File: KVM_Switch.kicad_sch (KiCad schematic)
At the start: 4 parts, among them J1 HDMI_A, J2 HDMI_A, U1 USB2514B_Bi, U2 STM32C011F4Px

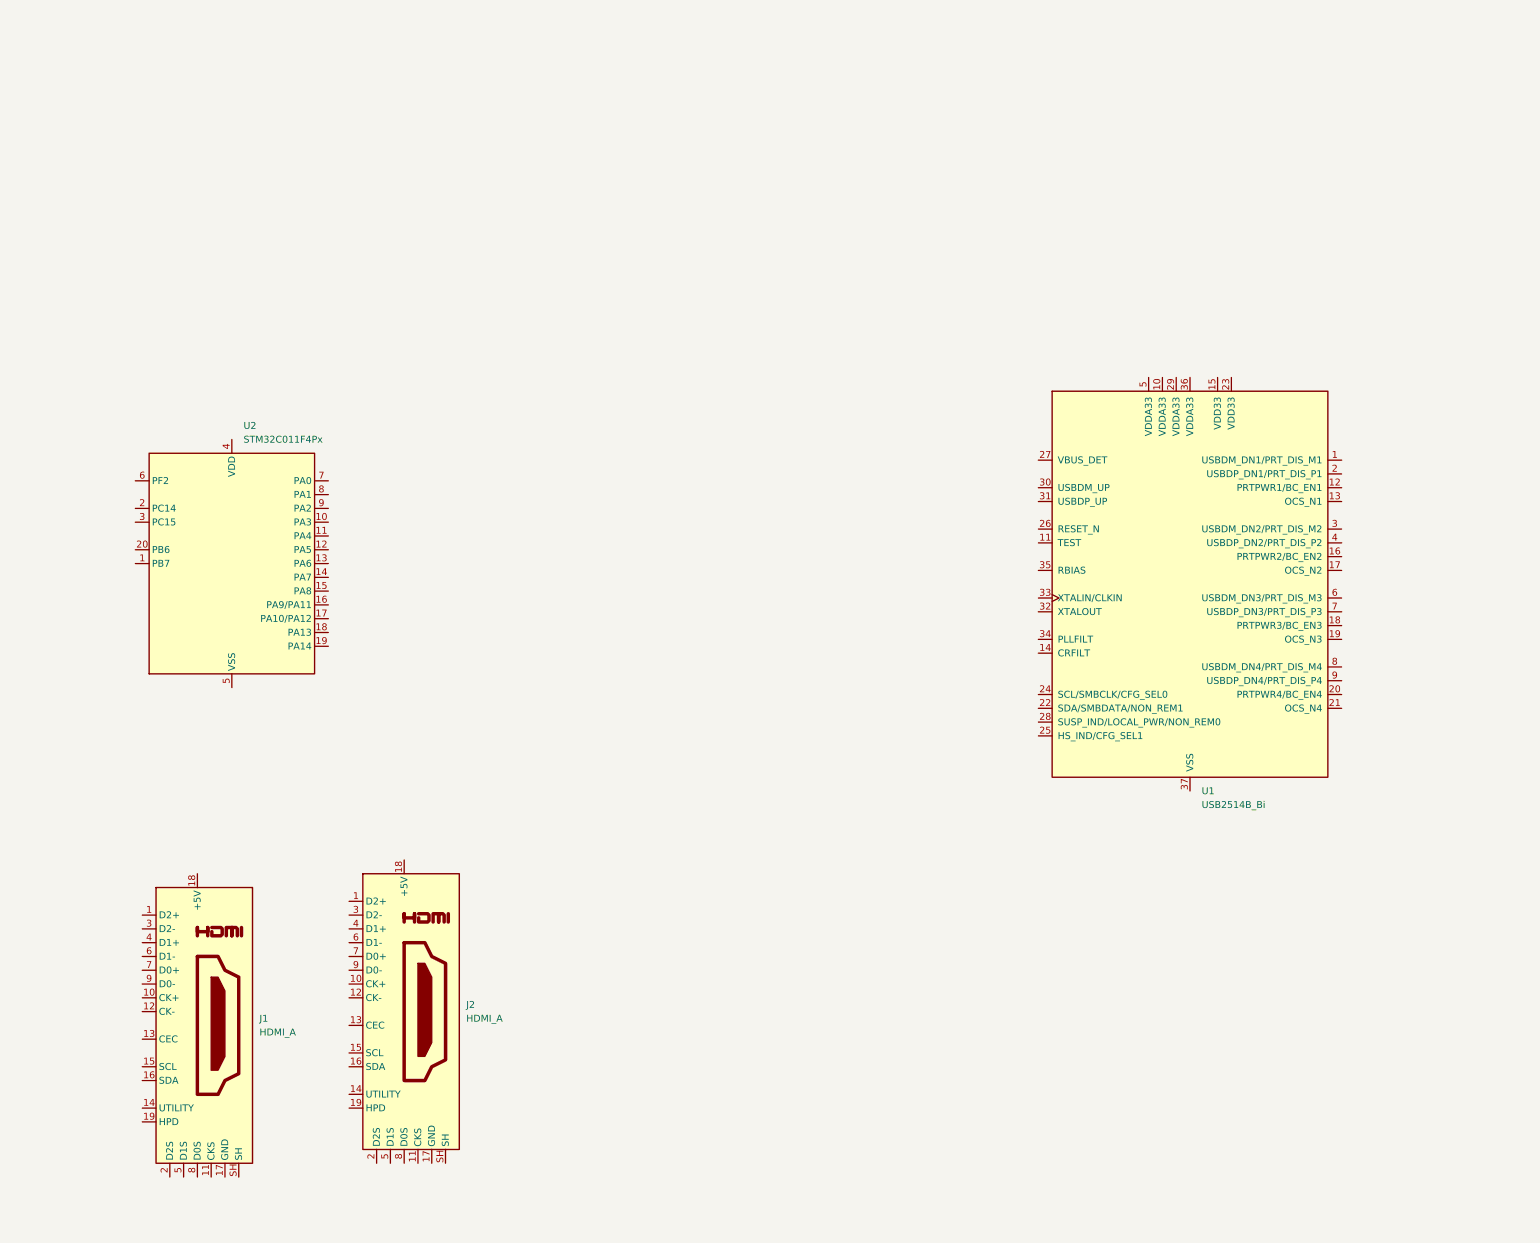
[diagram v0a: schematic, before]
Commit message: Added switching ICs and MCU
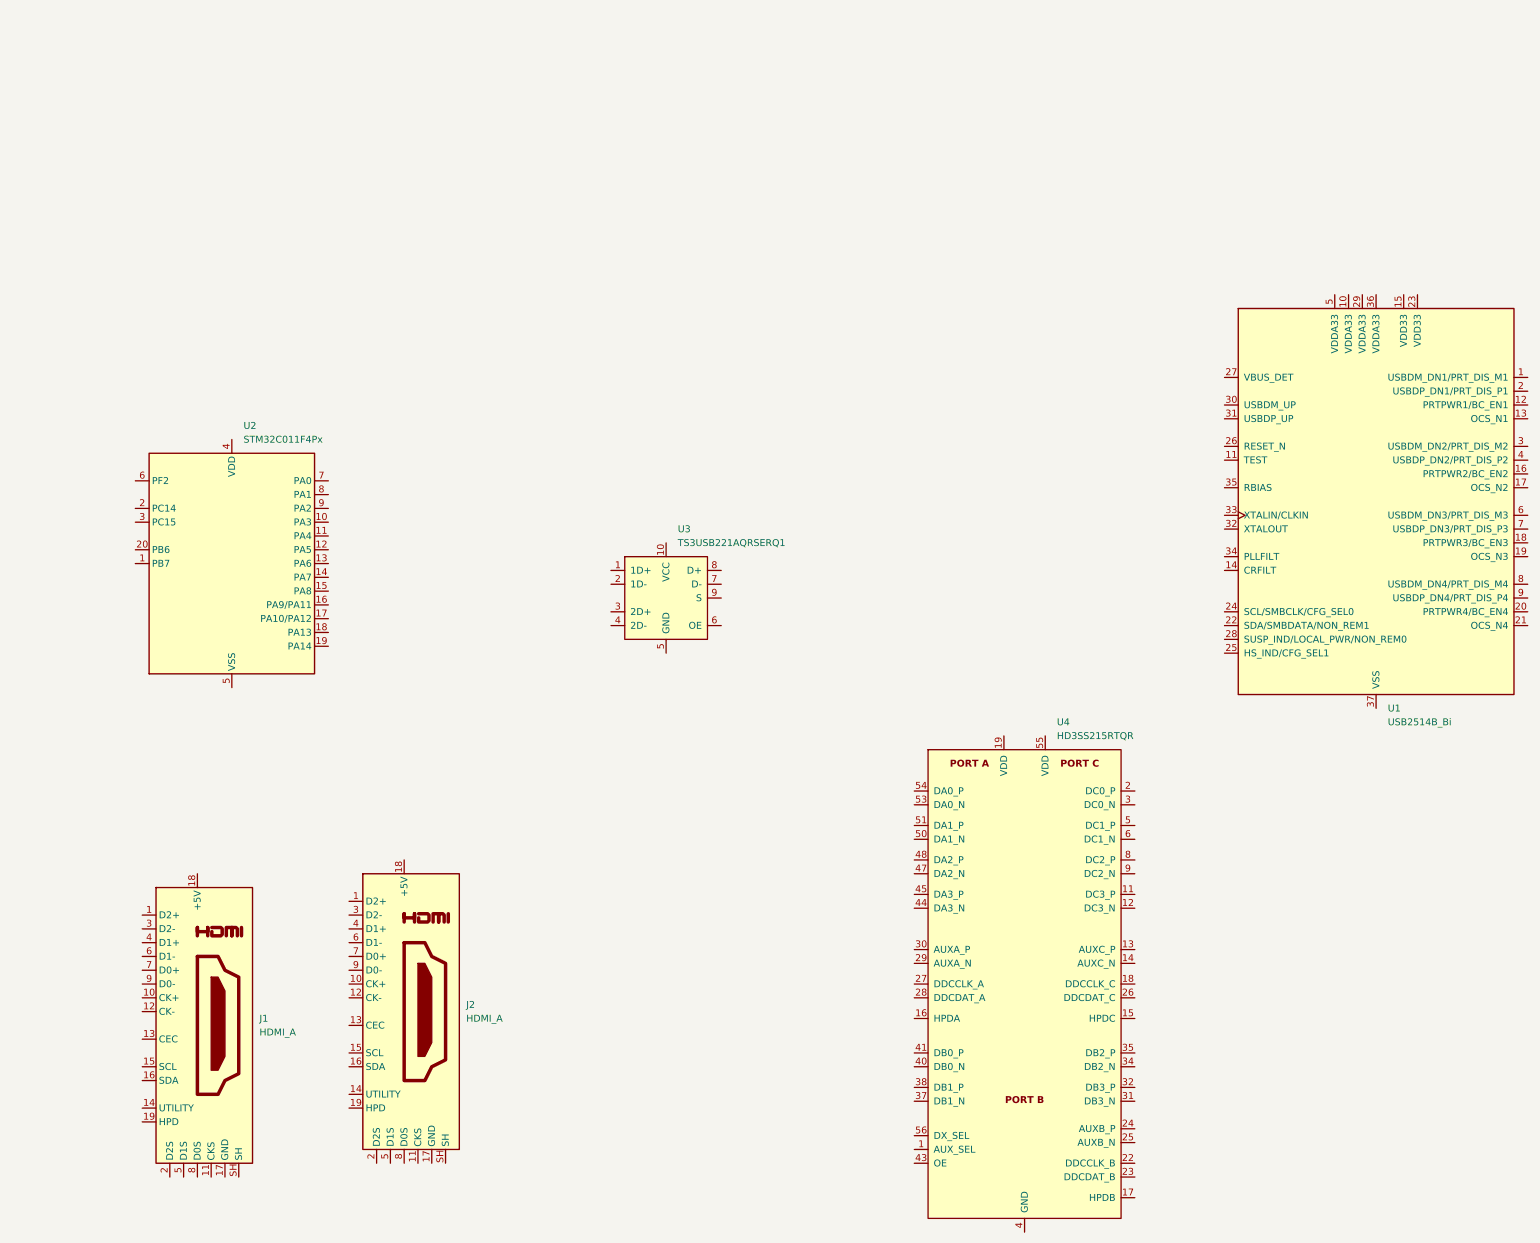
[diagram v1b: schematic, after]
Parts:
- added U3: TS3USB221AQRSERQ1, TS3USB221AQRSERQ1:TS3USB221AQRSERQ1, symbol TS3USB221AQRSERQ1:TS3USB221AQRSERQ1
- added U4: HD3SS215RTQR, Package_DFN_QFN:QFN-56-1EP_8x8mm_P0.5mm_EP4.3x4.3mm, symbol HD3SS215RTQR:HD3SS215RTQR
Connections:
- new net: U4.20 (NC), U4.21 (NC), U4.42 (NC)
- new net GND: U4.10 (GND), U4.33 (GND), U4.36 (GND), U4.39 (GND), U4.46 (GND), U4.49 (GND), U4.52 (GND), U4.57 (GND), U4.7 (GND)
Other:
- moved on the sheet: U1

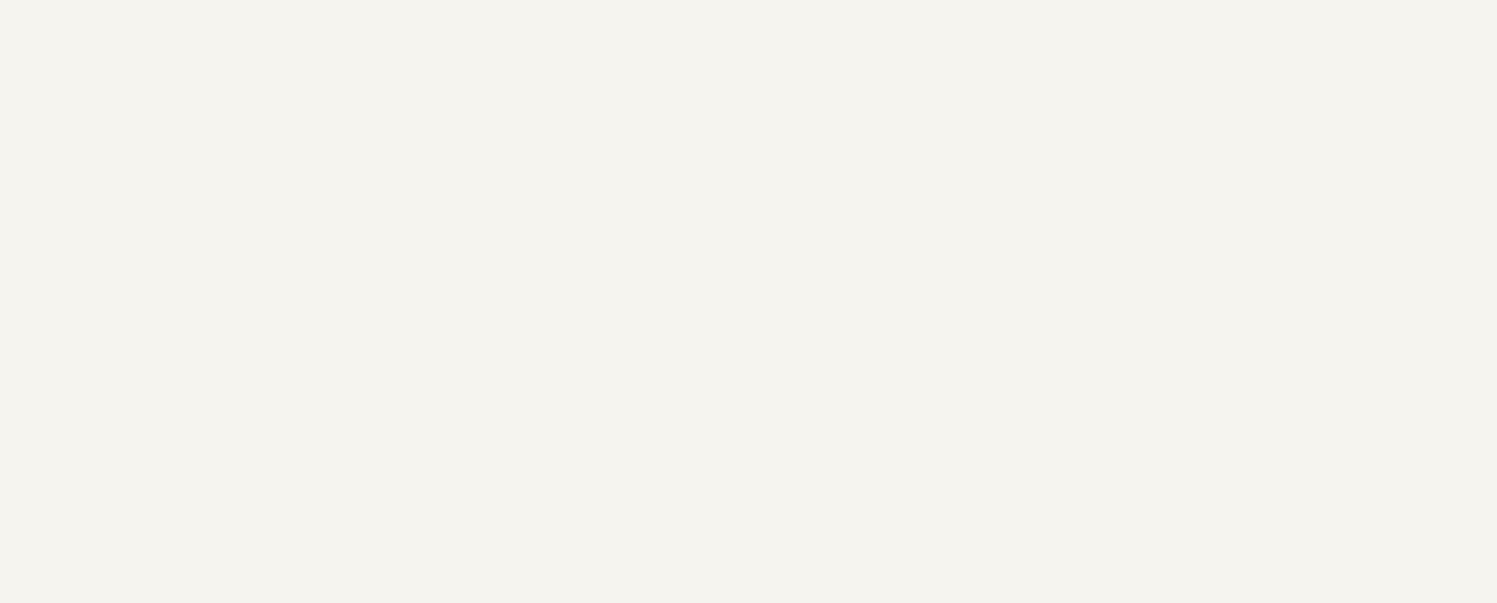
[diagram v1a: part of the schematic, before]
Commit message: USB-C connectors
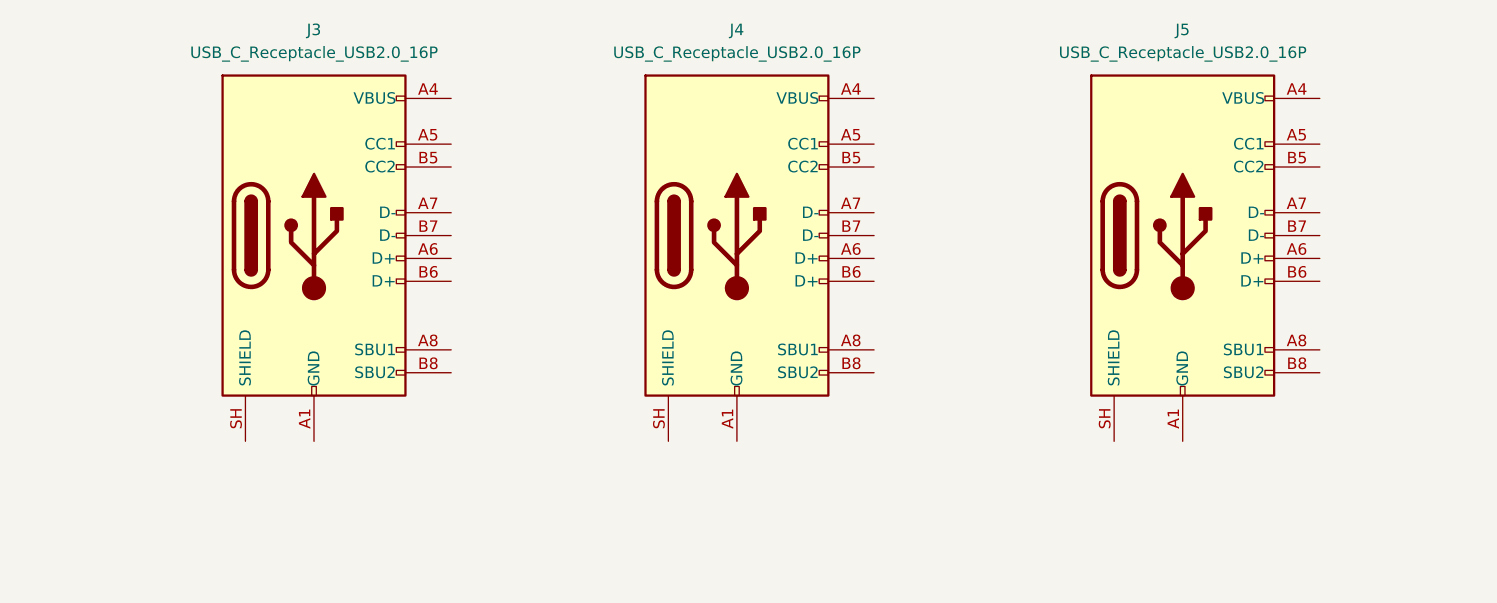
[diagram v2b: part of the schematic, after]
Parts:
- added J3, J4, J5: USB_C_Receptacle_USB2.0_16P, Connector_USB:USB_C_Receptacle_GCT_USB4105-xx-A_16P_TopMnt_Horizontal, symbol Connector:USB_C_Receptacle_USB2.0_16P
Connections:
- new net: J4.A1 (GND), J4.A12 (GND), J4.B1 (GND), J4.B12 (GND)
- new net: J4.A4 (VBUS), J4.A9 (VBUS), J4.B4 (VBUS), J4.B9 (VBUS)
- new net: J3.A1 (GND), J3.A12 (GND), J3.B1 (GND), J3.B12 (GND)
- new net: J3.A4 (VBUS), J3.A9 (VBUS), J3.B4 (VBUS), J3.B9 (VBUS)
- new net: J5.A1 (GND), J5.A12 (GND), J5.B1 (GND), J5.B12 (GND)
- new net: J5.A4 (VBUS), J5.A9 (VBUS), J5.B4 (VBUS), J5.B9 (VBUS)

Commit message: Moved stuff armound & added components
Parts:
- removed J1, J2: HDMI_A, Connector_Video:HDMI_A_Molex_208658-1001_Horizontal, symbol Connector:HDMI_A
- removed J3, J4, J5: USB_C_Receptacle_USB2.0_16P, Connector_USB:USB_C_Receptacle_GCT_USB4105-xx-A_16P_TopMnt_Horizontal, symbol Connector:USB_C_Receptacle_USB2.0_16P
- removed U1: USB2514B_Bi, Package_DFN_QFN:QFN-36-1EP_6x6mm_P0.5mm_EP3.7x3.7mm, symbol Interface_USB:USB2514B_Bi
- removed U2: STM32C011F4Px, Package_SO:TSSOP-20_4.4x6.5mm_P0.65mm, symbol MCU_ST_STM32C0:STM32C011F4Px
- removed U3: TS3USB221AQRSERQ1, TS3USB221AQRSERQ1:TS3USB221AQRSERQ1, symbol TS3USB221AQRSERQ1:TS3USB221AQRSERQ1
- removed U4: HD3SS215RTQR, Package_DFN_QFN:QFN-56-1EP_8x8mm_P0.5mm_EP4.3x4.3mm, symbol HD3SS215RTQR:HD3SS215RTQR
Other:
- added sheet HDMI_Switch (HDMI_Switch.kicad_sch)
- added sheet MCU (MCU.kicad_sch)
- added sheet Power (Power.kicad_sch)
- added sheet UBS_Hub (USB_Hub.kicad_sch)
- added sheet USB_Host_Select (USB_Host_Select.kicad_sch)

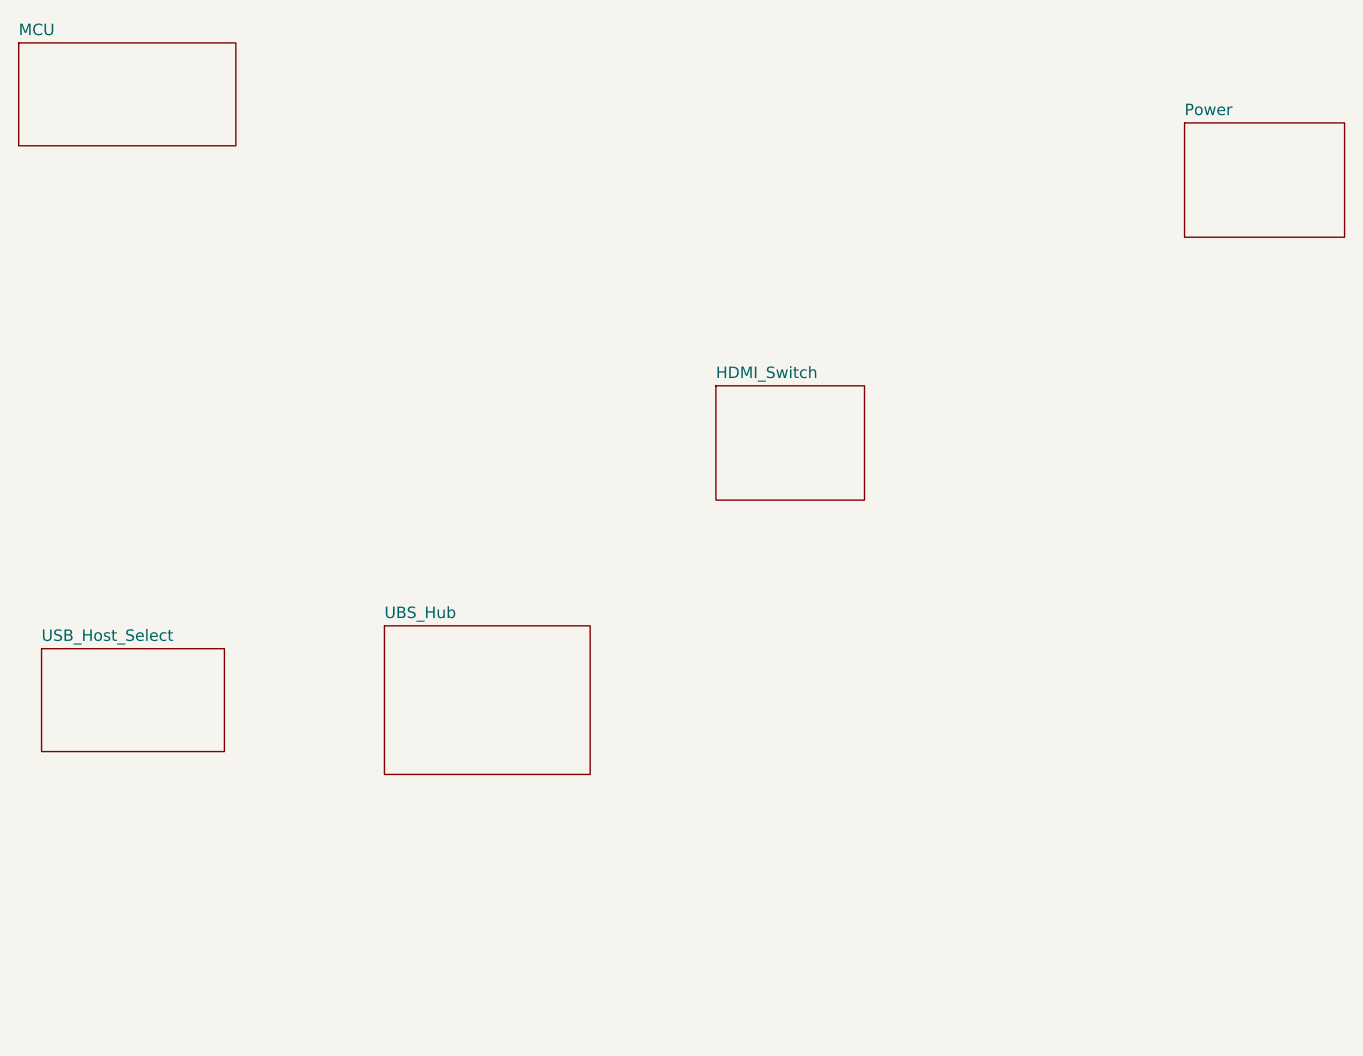
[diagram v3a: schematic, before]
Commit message: Better schematics structure & Hub sub-circuit connections
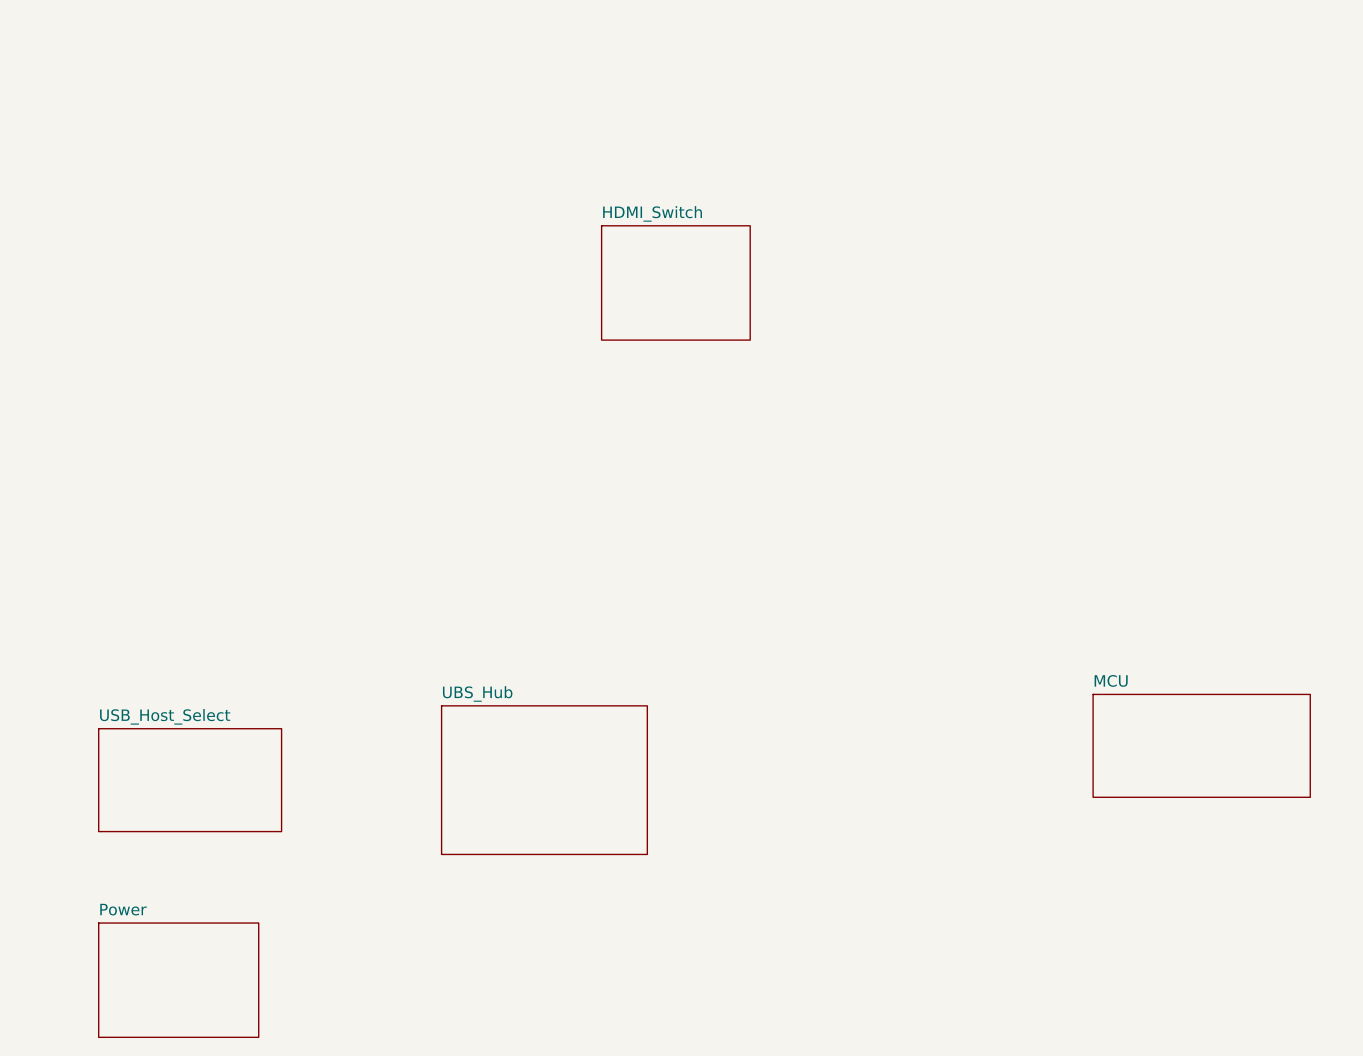
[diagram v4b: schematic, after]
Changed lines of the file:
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@@
 	)
 	(sheet
-		(at 91.44 96.52)
+		(at 97.79 105.41)
 		(size 22.86 16.51)
 		(exclude_from_sim no)
@@
 		)
 		(property "Sheetname" "UBS_Hub"
-			(at 91.44 95.8084 0)
+			(at 97.79 104.6984 0)
 			(show_name no)
 			(do_not_autoplace no)
@@
 		)
 		(property "Sheetfile" "USB_Hub.kicad_sch"
-			(at 91.44 113.6146 0)
+			(at 97.79 122.5046 0)
 			(hide yes)
 			(show_name no)
@@
 	)
 	(sheet
-		(at 180.34 40.64)
+		(at 59.69 129.54)
 		(size 17.78 12.7)
 		(exclude_from_sim no)
@@
 		)
 		(property "Sheetname" "Power"
-			(at 180.34 39.9284 0)
+			(at 59.69 128.8284 0)
 			(show_name no)
 			(do_not_autoplace no)
@@
 		)
 		(property "Sheetfile" "Power.kicad_sch"
-			(at 180.34 53.9246 0)
+			(at 59.69 142.8246 0)
 			(hide yes)
 			(show_name no)
@@
 	)
 	(sheet
-		(at 128.27 69.85)
+		(at 115.57 52.07)
 		(size 16.51 12.7)
 		(exclude_from_sim no)
@@
 		)
 		(property "Sheetname" "HDMI_Switch"
-			(at 128.27 69.1384 0)
+			(at 115.57 51.3584 0)
 			(show_name no)
 			(do_not_autoplace no)
@@
 		)
 		(property "Sheetfile" "HDMI_Switch.kicad_sch"
-			(at 128.27 83.1346 0)
+			(at 115.57 65.3546 0)
 			(hide yes)
 			(show_name no)
@@
 	)
 	(sheet
-		(at 53.34 99.06)
+		(at 59.69 107.95)
 		(size 20.32 11.43)
 		(exclude_from_sim no)
@@
 		)
 		(property "Sheetname" "USB_Host_Select"
-			(at 53.34 98.3484 0)
+			(at 59.69 107.2384 0)
 			(show_name no)
 			(do_not_autoplace no)
@@
 		)
 		(property "Sheetfile" "USB_Host_Select.kicad_sch"
-			(at 53.34 111.0746 0)
+			(at 59.69 119.9646 0)
 			(hide yes)
 			(show_name no)
@@
 	)
 	(sheet
-		(at 50.8 31.75)
+		(at 170.18 104.14)
 		(size 24.13 11.43)
 		(exclude_from_sim no)
@@
 		)
 		(property "Sheetname" "MCU"
-			(at 50.8 31.0384 0)
+			(at 170.18 103.4284 0)
 			(show_name no)
 			(do_not_autoplace no)
@@
 		)
 		(property "Sheetfile" "MCU.kicad_sch"
-			(at 50.8 43.7646 0)
-			(hide yes)
-			(show_name no)
+			(at 170.18 116.1546 0)
+			(hide yes)
+			(show_name no)
